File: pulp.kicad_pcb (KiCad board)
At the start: 2 copper layers, 88.9 x 38.1 mm, 71 parts, among them J1 Conn_Coaxial, J2 Conn_01x02_Pin, J3 Conn_01x02_Pin, J4 Conn_01x03_Pin, J5 Conn_01x03_Pin, J6 Conn_01x09_Pin, J7 USB_C_Receptacle, J8 Conn_01x02_Pin, Q1 BSS138, Q2 BSS138, Q3 BSS138, SW1 SW_Push, SW2 SW_Push, U1 HMC5883L, U2 RP2040, U3 MAX-M8Q, U4 AP7361C-33E, U5 W25Q128JVS, U6 BD33FC0FP, X2 ASE-12.0MHz

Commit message: edits to pcb board
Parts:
- moved D3 157.4 mm to (231.1, 99.1)
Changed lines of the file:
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@@
   )
   (footprint "LED_SMD:LED_RGB_1210" (layer "F.Cu")
-    (at 77.88 63.1925)
+    (at 231.14 99.06)
     (descr "RGB LED 3.2x2.7mm http://www.avagotech.com/docs/AV02-0610EN")
     (tags "LED 3227")
@@
     (fp_line (start 3.5 -3.5) (end 3.5 3.5)
       (stroke (width 0.1) (type solid)) (layer "F.Fab"))
-    (pad "1" thru_hole roundrect (at 0 0 90) (size 2.3 2.3) (drill 1.5) (layers "*.Cu" "*.Mask") (remove_unused_layers) (keep_end_layers) (zone_layer_connections "F.Cu") (roundrect_rratio 0.087)
+    (pad "1" thru_hole roundrect (at 0 0 90) (size 2.3 2.3) (drill 1.5) (layers "*.Cu" "*.Mask") (remove_unused_layers) (keep_end_layers) (zone_layer_connections) (roundrect_rratio 0.087)
       (net 14 "Net-(J1-In)") (pinfunction "In") (pintype "passive"))
     (pad "2" thru_hole circle (at -2.54 -2.54 90) (size 2.5 2.5) (drill 1.7) (layers "*.Cu" "*.Mask") (remove_unused_layers) (keep_end_layers) (zone_layer_connections)

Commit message: finished pcb layout
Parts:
- removed C10, C9: 1uF, Capacitor_SMD:C_0201_0603Metric
- removed J8: Conn_01x02_Pin, Connector_AMASS:AMASS_XT60-F_1x02_P7.20mm_Vertical
- removed U6: BD33FC0FP, Package_TO_SOT_SMD:TO-252-2
- added D4: 1A, Diode_SMD:D_1812_4532Metric, F.Cu at (70.6, 69.5)
- J1: footprint Connector_Coaxial:SMA_Amphenol_901-143_Horizontal -> Connector_Coaxial:U.FL_Molex_MCRF_73412-0110_Vertical
- moved D3 138.9 mm to (93.6, 79.8)
- moved J5 133.7 mm to (37.4, 51.5)
- moved C16 131.0 mm to (93.1, 72.5), turned to -90 degrees
- moved C1 129.1 mm to (110.5, 59.9)
- moved C2 129.1 mm to (114.3, 63.0)
- moved R1 129.1 mm to (108.6, 62.4)
- moved R2 129.1 mm to (108.6, 61.1)
- moved U1 129.1 mm to (111.8, 63.0)
- moved C27 123.6 mm to (91.2, 67.3)
- moved J6 123.6 mm to (94.6, 45.9)
- moved J7 123.6 mm to (70.8, 77.0)
- moved R10 123.6 mm to (99.7, 70.7)
- moved R13 123.6 mm to (91.7, 50.9)
- moved R14 123.6 mm to (91.7, 52.1)
- moved U4 123.6 mm to (78.1, 64.3)
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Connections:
- J2 pad 1: I2C_SDA 1 -> I2C_SCL 1
- J2 pad 2: I2C_SCL 1 -> I2C_SDA 1
- J3 pad 1: I2C_SDA 0 -> I2C_SCL 0
- J3 pad 2: I2C_SCL 0 -> I2C_SDA 0
- J4 pad 3: BATT_V -> 5V
- J5 pad 3: BATT_V -> 5V
- J7 pad A4: 5V -> Net-(D4-A)
- J7 pad A9: 5V -> Net-(D4-A)
- J7 pad B4: 5V -> Net-(D4-A)
- J7 pad B9: 5V -> Net-(D4-A)
- R17 pad 1: /USB_D- -> /USB_D+
- R17 pad 2: /USB_D- -> Net-(U2-USB_DP)
- R18 pad 1: /USB_D+ -> Net-(U2-USB_DM)
- R18 pad 2: /USB_D+ -> /USB_D-
- U2 pad 46: /USB_D+ -> Net-(U2-USB_DM)
- U2 pad 47: /USB_D- -> Net-(U2-USB_DP)
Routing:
- net GND: track 0.00 -> 100.8 mm, vias 0 -> 50
- net 5V: track 42.8 -> 129.3 mm, vias 2 -> 7
- net BATT_V: track 77.5 -> 0.00 mm, vias 2 -> 0
- net /~{RST}: track 0.00 -> 61.7 mm, vias 0 -> 2
- net 3V3: track 111.4 -> 165.1 mm, vias 6 -> 10
- net /Q_SS: track 11.1 -> 62.4 mm, vias 0 -> 2
- net Net-(U2-USB_DP): track 0.00 -> 37.6 mm, vias 0 -> 2
- net Net-(U2-USB_DM): track 0.00 -> 36.8 mm, vias 0 -> 2
- net /MAX_8C GNSS/TXD: track 0.00 -> 35.9 mm, vias 0 -> 2
- net /MAX_8C GNSS/RXD: track 0.00 -> 34.8 mm, vias 0 -> 2
- net PWM_RIGHT: track 98.1 -> 66.0 mm
- net PWM_LEFT: track 64.4 -> 93.4 mm, vias 0 -> 2
- net /LED_B: track 0.00 -> 25.7 mm, vias 0 -> 2
- net /USB_D+: track 0.00 -> 20.0 mm, vias 0 -> 2
- net /LED_G: track 0.00 -> 16.3 mm
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- added copper zone on B.Cu, net GND
- added copper zone on F.Cu, net GND
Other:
- board size 88.9 x 38.1 mm -> 84 x 38.1 mm
- board text added: "3V3"
- board text added: "5V"
- board text added: "GND"
- board text added: "GP0"
- board text added: "GP1"
- board text added: "GP2"
- board text added: "GP3"
- board text added: "GP4"
- board text added: "GP5"
- board text added: "I2C_SCL 0"
- board text added: "I2C_SCL 1"
- board text added: "I2C_SDA 0"
- board text added: "I2C_SDA 1"
- board text added: "PWM_L"
- board text added: "PWM_R"
- board text added: "VIN"

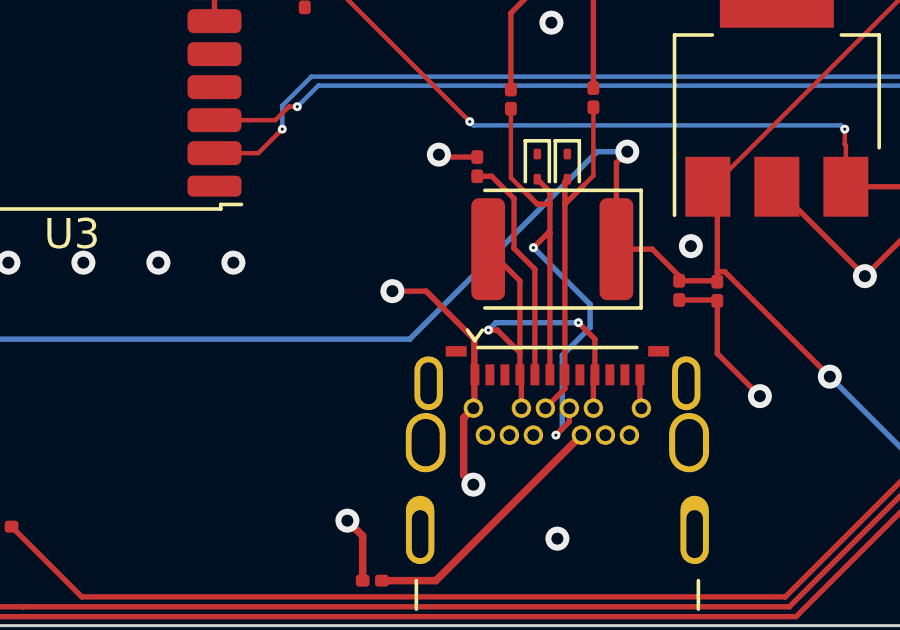
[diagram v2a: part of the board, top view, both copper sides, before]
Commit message: agged ground VIA to help remove island
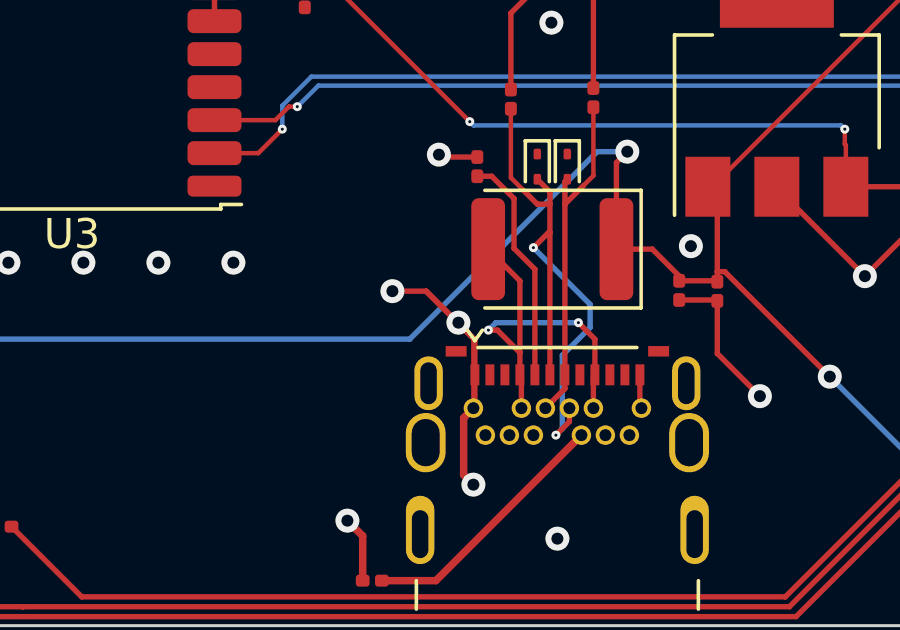
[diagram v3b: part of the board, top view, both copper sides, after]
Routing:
- net GND: vias 50 -> 51
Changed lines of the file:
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@@
 		(tags "resistor")
 		(property "Reference" "R17"
-			(at 0 -1.05 270)
+			(at 0 -1.05 -90)
 			(layer "F.SilkS")
 			(hide yes)
@@
 		)
 		(property "Value" "27"
-			(at 0 1.05 270)
+			(at 0 1.05 -90)
 			(layer "F.Fab")
 			(effects
@@
 		)
 		(fp_text user "${REFERENCE}"
-			(at 0 -0.680001 270)
+			(at 0 -0.680001 -90)
 			(layer "F.Fab")
 			(effects
@@
 	(segment
 		(start 68.015 72.54)
-		(end 66.425 70.95)
+		(end 67.5 72.025)
 		(width 0.18)
 		(layer "F.Cu")
@@
 	)
 	(segment
+		(start 67.5 72)
+		(end 67.475 72)
+		(width 0.18)
+		(layer "F.Cu")
+		(net 2)
+	)
+	(segment
 		(start 68.05 73.74)
 		(end 68.05 72.575)
@@
 	)
 	(segment
+		(start 67.475 72)
+		(end 66.425 70.95)
+		(width 0.18)
+		(layer "F.Cu")
+		(net 2)
+	)
+	(segment
 		(start 97 62.2)
 		(end 97 63.25)
@@
 	)
 	(segment
+		(start 67.5 72.025)
+		(end 67.5 72)
+		(width 0.18)
+		(layer "F.Cu")
+		(net 2)
+	)
+	(segment
 		(start 96 67.401544)
 		(end 96 66.6875)
@@
 		(net 2)
 	)
+	(via
+		(at 67.5 72)
+		(size 0.8)
+		(drill 0.4)
+		(layers "F.Cu" "B.Cu")
+		(net 2)
+	)
